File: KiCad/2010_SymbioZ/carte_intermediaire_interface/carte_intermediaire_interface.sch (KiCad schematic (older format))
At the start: 10 parts

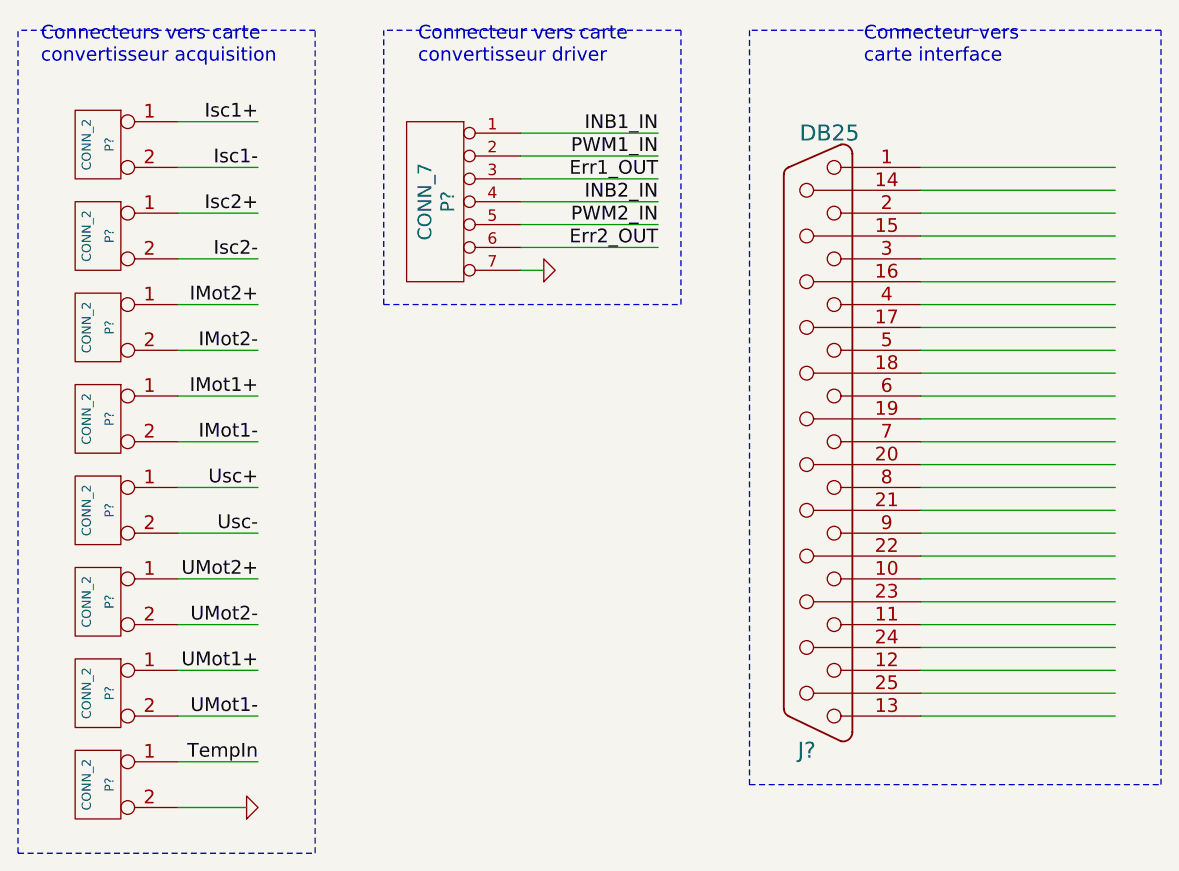
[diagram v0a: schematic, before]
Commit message: 
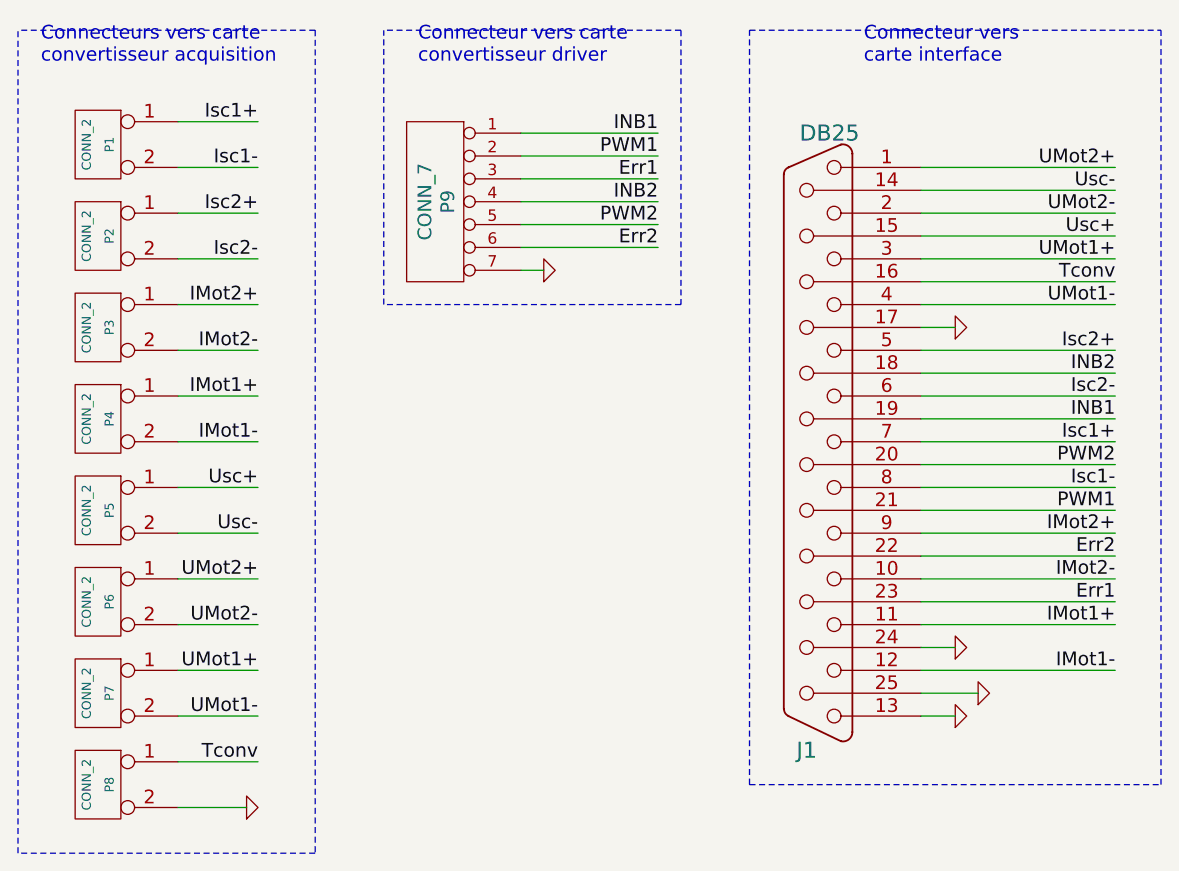
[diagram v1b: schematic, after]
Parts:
- gave numbers to parts that had none: 10
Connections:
- net labels added: Err1, Err2, INB1, INB2, PWM1, PWM2, Tconv
- net labels removed: Err1_OUT, Err2_OUT, INB1_IN, INB2_IN, PWM1_IN, PWM2_IN, TempIn
